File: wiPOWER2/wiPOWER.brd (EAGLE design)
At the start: 31.8 x 61.6 mm, 32 parts, among them IC1 AMS1117, IC2 ACS724, J3 USB, K1 G5LE, Q1 S8050

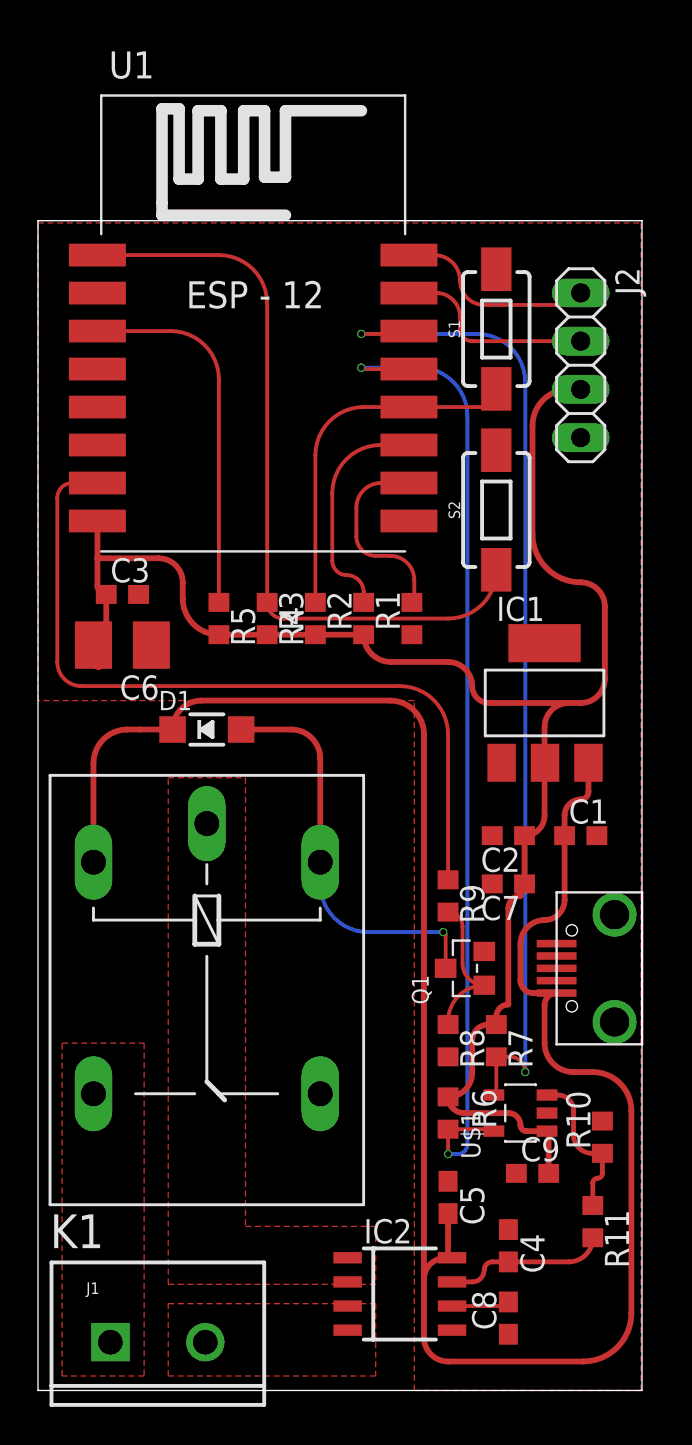
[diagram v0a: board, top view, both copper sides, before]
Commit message: wiPOWER2: Add power traces
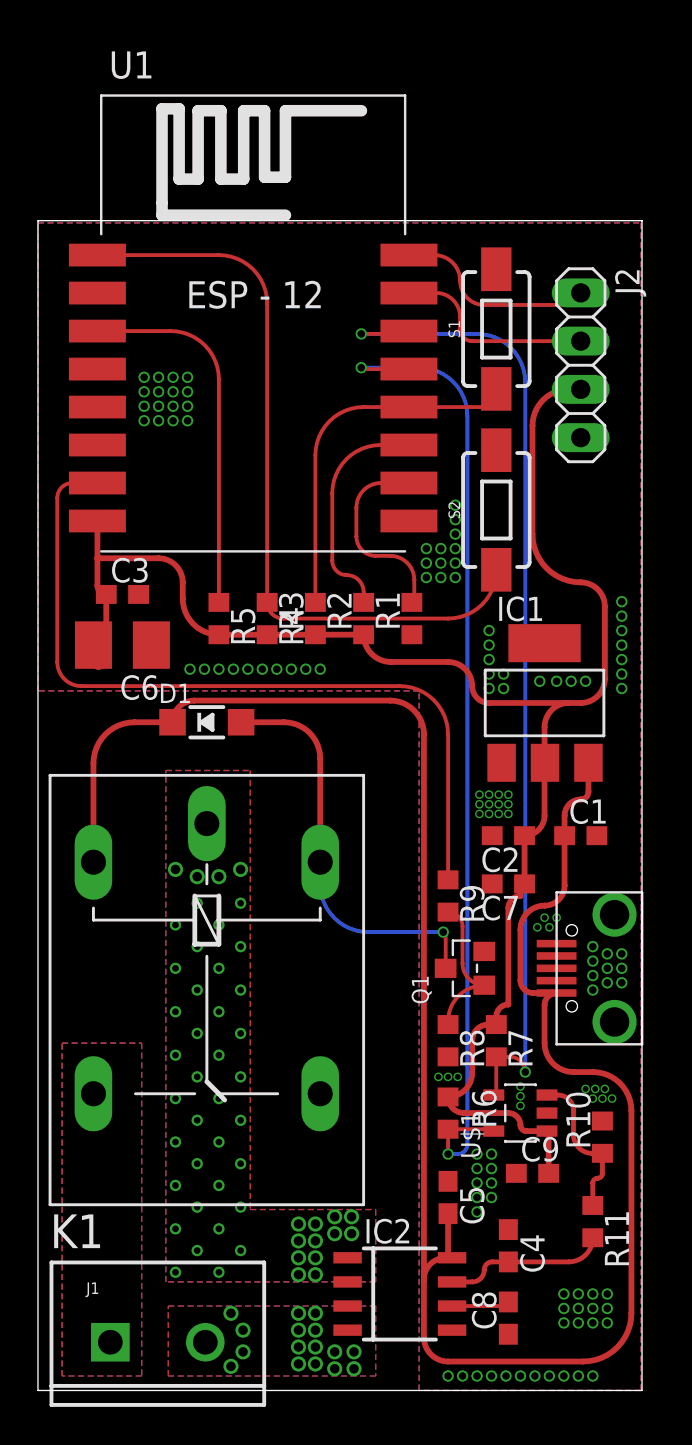
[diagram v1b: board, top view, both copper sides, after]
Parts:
- moved D1 0.38 mm to (8.89, 35.2)
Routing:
- added copper zone on layer 16, net GND
- added copper zone on layer 16, net IP+
- added copper zone on layer 16, net IP-
- added copper zone on layer 16, net PRE_IP+
